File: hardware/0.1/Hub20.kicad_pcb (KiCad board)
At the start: 4 copper layers, 84.2 x 118.2 mm, 169 parts, among them J1 USB_C_Receptacle_USB2.0, J2 USB_C_Receptacle_USB2.0, J3 USB_C_Receptacle_USB2.0, J4 USB_C_Receptacle_USB2.0, Q1 DTC123J, Q2 BSS138, SW1 SW_Push, SW10 MX_RGB, SW11 MX_RGB, SW12 MX_RGB, SW13 Encoder_MX_RGB, SW14 MX_RGB, SW15 MX_RGB, SW16 MX_RGB, SW17 MX_RGB, SW18 MX_RGB, SW19 MX_RGB, SW2 MX_RGB, SW20 MX_RGB, SW21 MX_RGB, SW22 MX_RGB, SW23 MX_RGB, SW3 MX_RGB, SW4 MX_RGB, SW5 MX_RGB, SW6 MX_RGB, SW7 Encoder_MX_RGB, SW8 MX_RGB, SW9 MX_RGB, U1 AP2112K-3.3, U2 USBLC6-2SC6, U3 STM32F072C8Tx, U4 CY7C65632-28LTXCT, U5 24LC02, U6 USBLC6-2SC6, U7 USBLC6-2SC6, U8 USBLC6-2SC6, Y1 12MHz

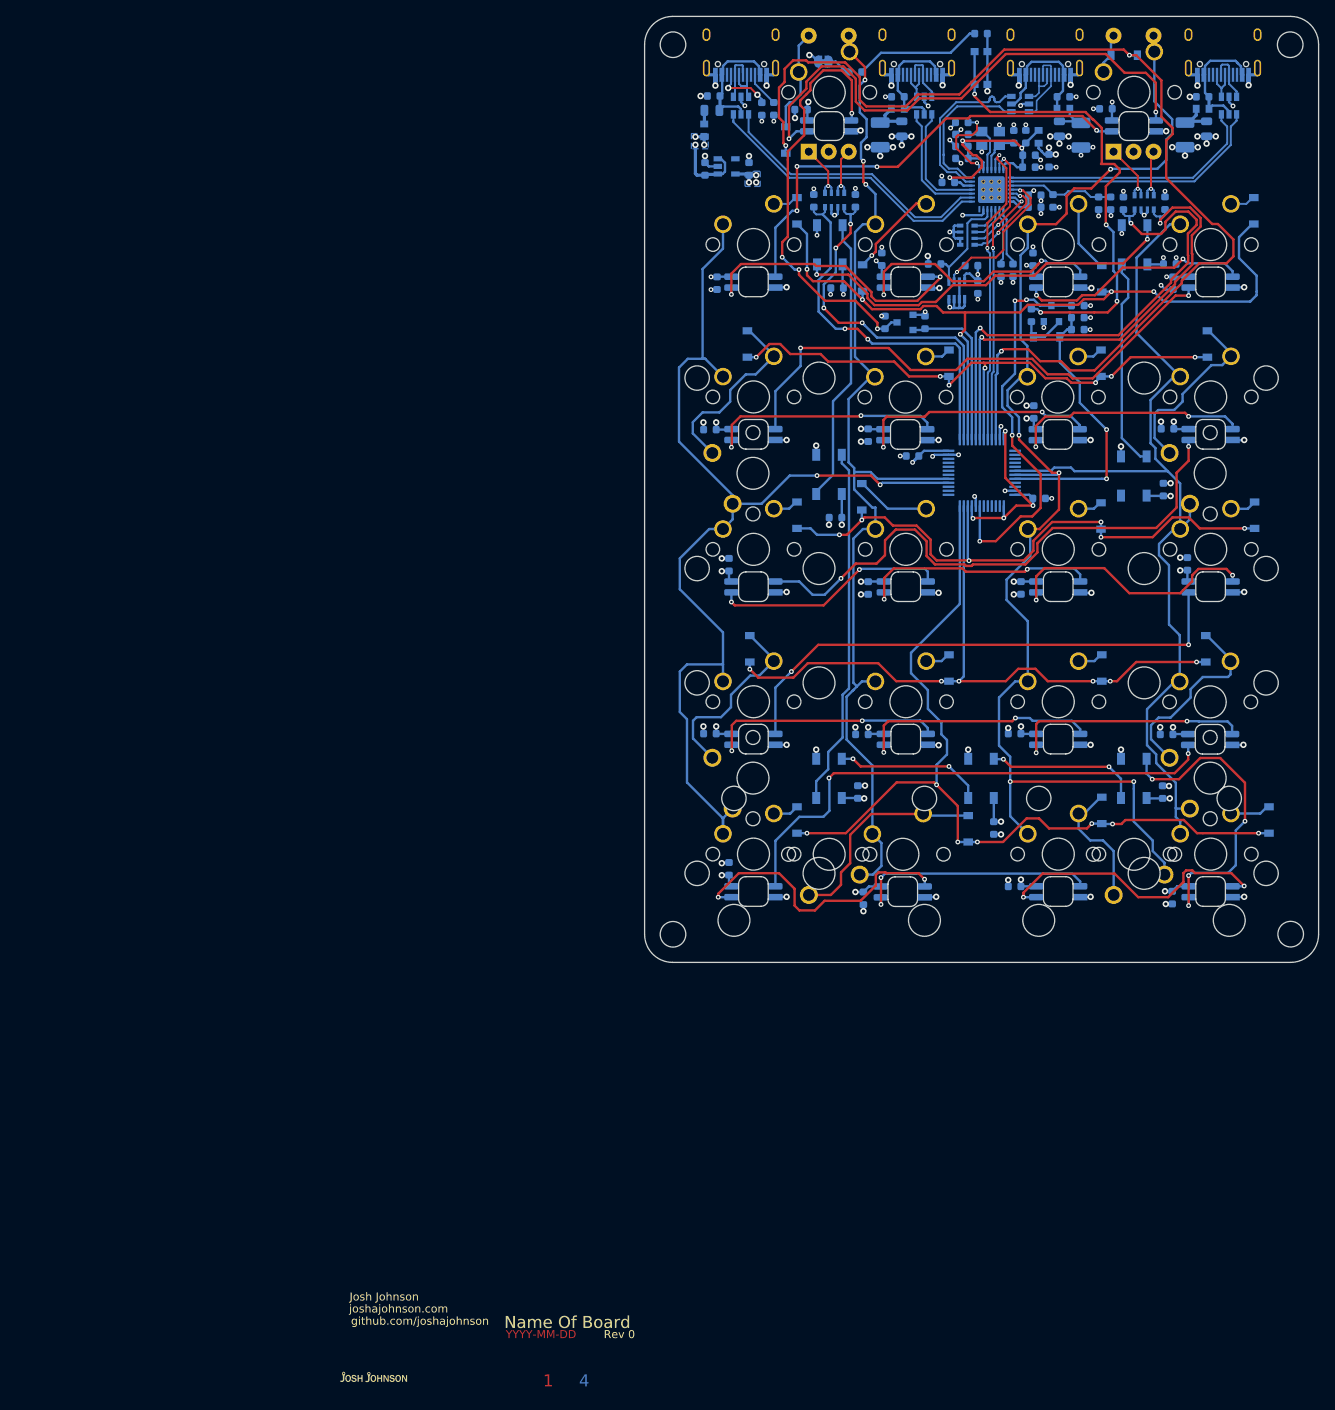
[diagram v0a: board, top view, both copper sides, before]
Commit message: clean up routing, design review TODO
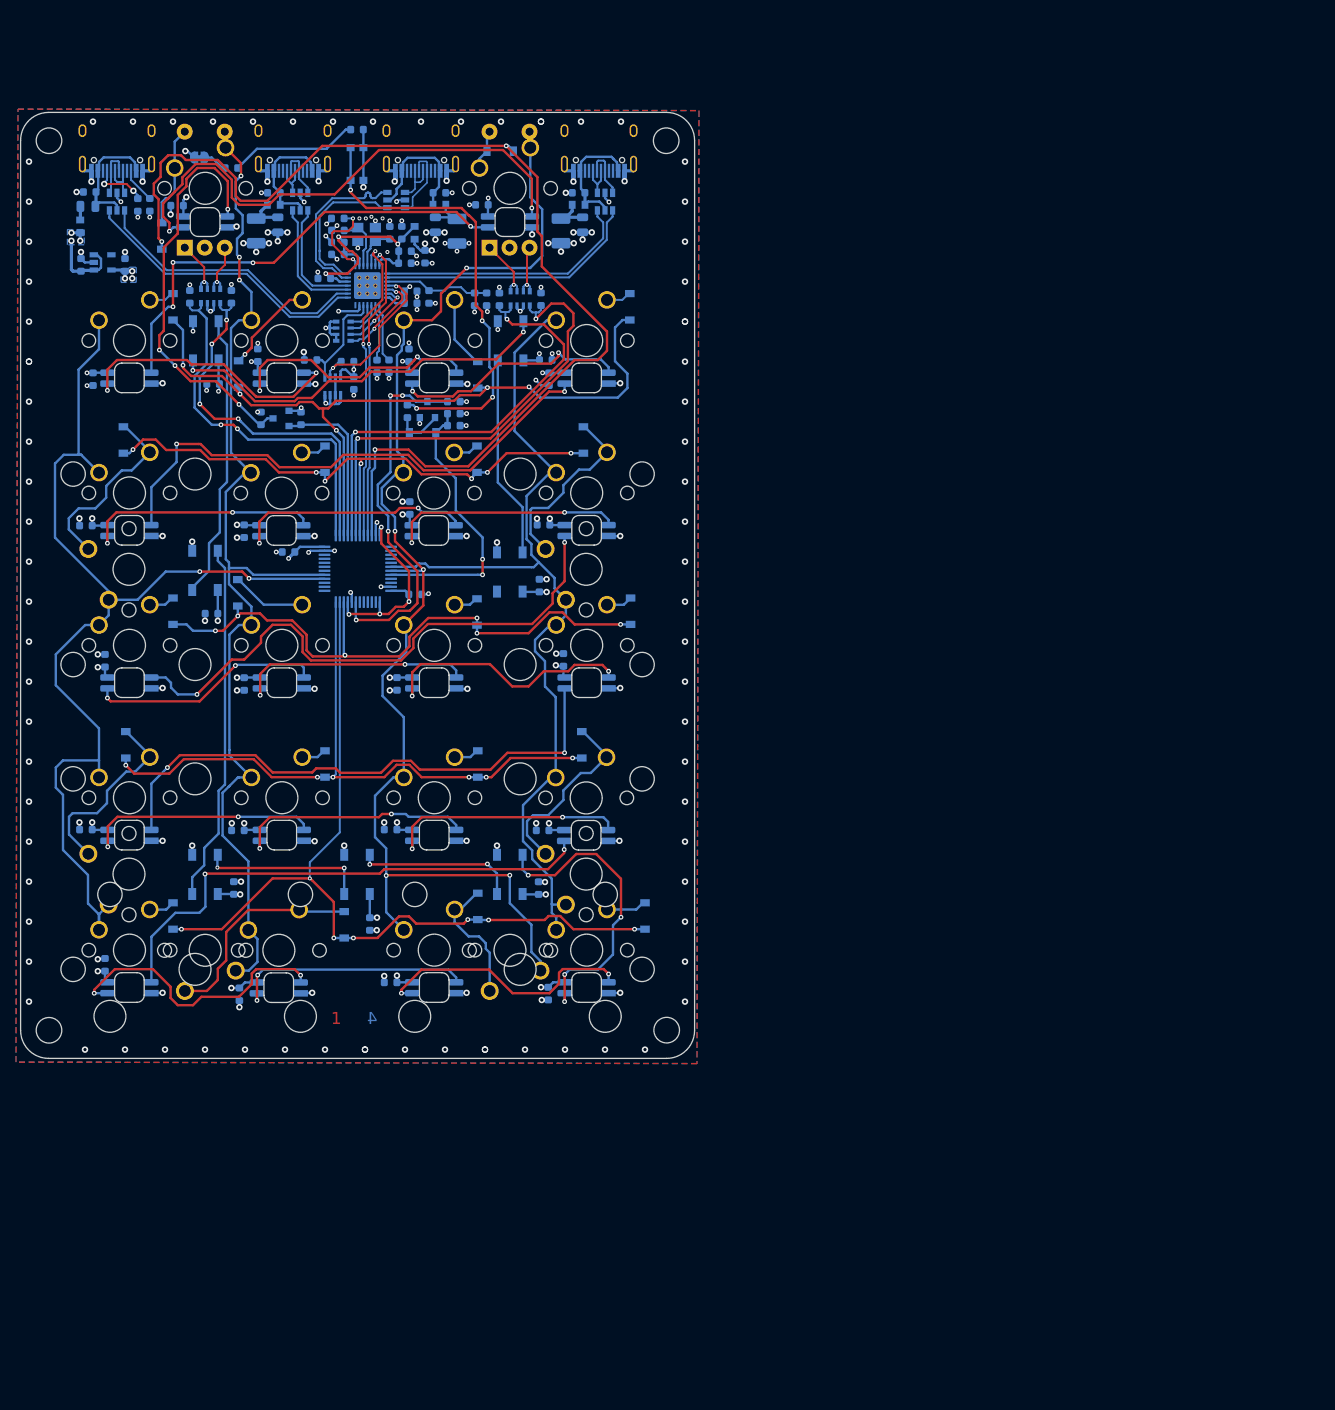
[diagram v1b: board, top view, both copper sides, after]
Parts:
- added LOGO5: OSHW, josh-logos:OSHW_Logo_3.6x3.6_F.Mask, B.Cu at (121.4, 111.1)
- LOGO1, LOGO2, LOGO3: moved to B.Cu
- moved LOGO3 83.8 mm to (133.0, 110.7), turned to 180 degrees
- moved C26 78.9 mm to (126.3, 146.1)
- moved C31 78.9 mm to (126.1, 125.6)
- moved C33 78.9 mm to (107.1, 125.5)
- moved C35 78.9 mm to (125.6, 132.8)
- moved C39 78.9 mm to (142.6, 137.3)
- moved C5 78.9 mm to (147.5, 66.2)
- moved C52 78.9 mm to (125.3, 58.9)
- moved C6 78.9 mm to (107.1, 87.5)
- moved D1 78.9 mm to (149.2, 75.9)
- moved D17 78.9 mm to (122.1, 64.4)
- moved D18 78.9 mm to (156.1, 68.7)
- moved D23 78.9 mm to (160.2, 64.4)
- moved D24 78.9 mm to (158.9, 40.7)
- moved D29 78.9 mm to (177.0, 136.3)
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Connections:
- U3 pad 11: /R4 -> /R5
- U3 pad 12: /R5 -> /R4
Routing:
- net /ENC2A_DB: track 64.9 -> 56.9 mm
- net +3V3: track 210.2 -> 214.7 mm
- net /C2: track 163.4 -> 159.0 mm
- net /L_R3: track 66.2 -> 70.2 mm
- net /R5: track 110.0 -> 106.1 mm
- net /C3: track 116.3 -> 113.0 mm
- net Net-(SW18-Pad4): track 36.3 -> 33.3 mm
- net /nRST: track 49.7 -> 46.9 mm
- net Net-(R1-Pad2): track 59.7 -> 57.0 mm
- net /R0: track 142.7 -> 140.5 mm
- net /LED_5V: track 54.2 -> 52.0 mm
- net Net-(D3-Pad2): track 18.7 -> 20.7 mm
- net Net-(SW13-Pad1): track 68.2 -> 66.8 mm
- net /ENC2B_DB: track 59.8 -> 58.4 mm
- net Net-(D23-Pad2): track 26.4 -> 25.3 mm
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- added copper zone on B.Cu, net GND
- added copper zone on F.Cu, net GND
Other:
- outline, holes or cut-outs redrawn

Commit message: designs off to fab
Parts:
- added C28: 1u, Capacitor_SMD:C_0603_1608Metric, B.Cu at (132.5, 92.3)
- added C32: 1u, Capacitor_SMD:C_0603_1608Metric, B.Cu at (141.1, 101.5)
- added C34: 1u, Capacitor_SMD:C_0603_1608Metric, B.Cu at (148.2, 97.6)
- added C36: 100n, Capacitor_SMD:C_0603_1608Metric, B.Cu at (141.1, 100.0)
- added C38: 100n, Capacitor_SMD:C_0603_1608Metric, B.Cu at (143.8, 86.2)
- added C40: 100n, Capacitor_SMD:C_0603_1608Metric, B.Cu at (143.8, 99.6)
- U5: footprint Package_TO_SOT_SMD:SOT-23-8 -> Package_DFN_QFN:DFN-8-1EP_3x2mm_P0.5mm_EP1.36x1.46mm
- moved U5 1.03 mm to (138.2, 71.1)
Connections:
- U4 pad 27: +5V -> (no net)
- U4 pad 28: (no net) -> +3V3
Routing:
- net +3V3: track 214.7 -> 232.0 mm
- net +5V: track 109.0 -> 105.8 mm
- net GND: track 172.7 -> 174.2 mm, vias 206 -> 254
- net /USB Hub/SDA: track 13.2 -> 14.0 mm
- net /nRST: track 46.9 -> 46.2 mm
- net /USB Hub/SCL: track 20.4 -> 20.9 mm
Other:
- board text added: "Computer"
- board text added: "JLCJLCJLC"
- board text added: "LED"
- board text added: "PWR"
- board text added: "RST"

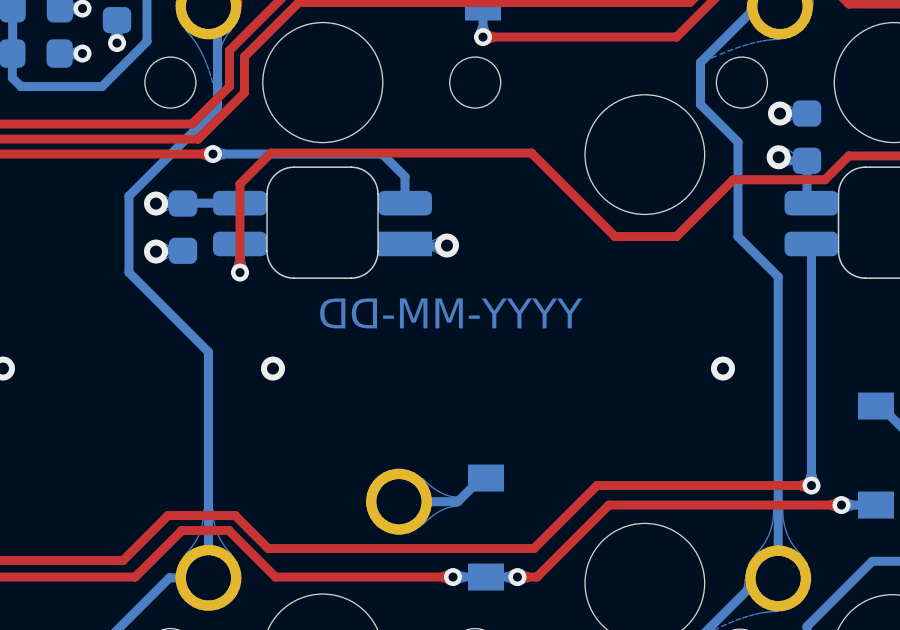
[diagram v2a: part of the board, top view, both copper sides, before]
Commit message: fit label locations
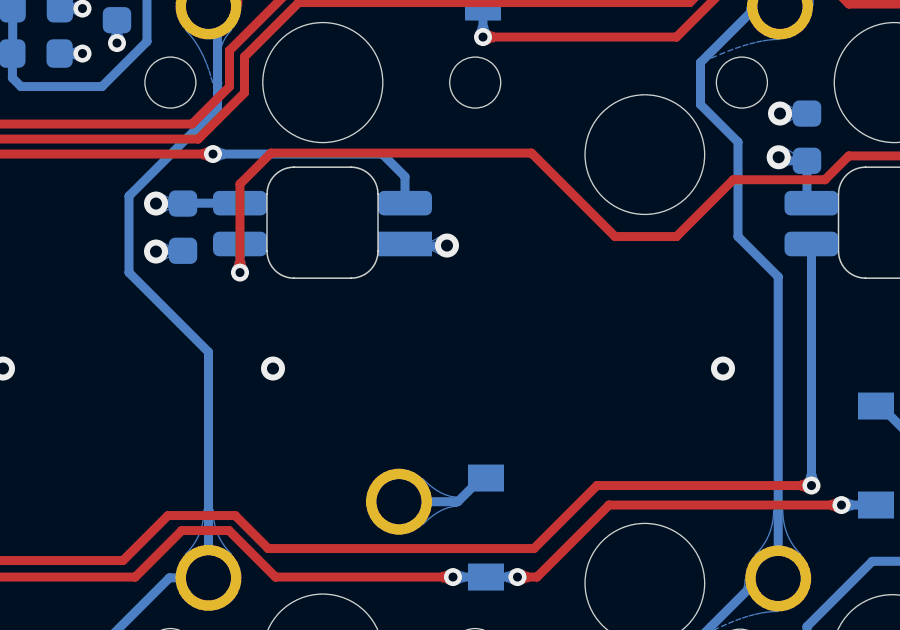
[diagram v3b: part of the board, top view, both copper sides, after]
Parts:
- removed LOGO3: Josh-Logo, josh-logos:josh-johnson-logo-8_6x1_5
